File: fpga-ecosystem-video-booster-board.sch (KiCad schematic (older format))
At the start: 91 parts, among them J1 0473460001, J10 61300411121, J2 HDMI-PE10-19-LF, J3 HDMI-PE10-19-LF, J4 M20-9990246, J5 M20-9990246, J6 685119134923_, J7 M20-9990246, J8 M20-9990246, J9 685119134923_, Q1 BSS138-7-F, Q2 BSS138-7-F, U1 PTN3363, U2 EFM32HG309, U3 PTN3363, U4 LP2985-33DBVR

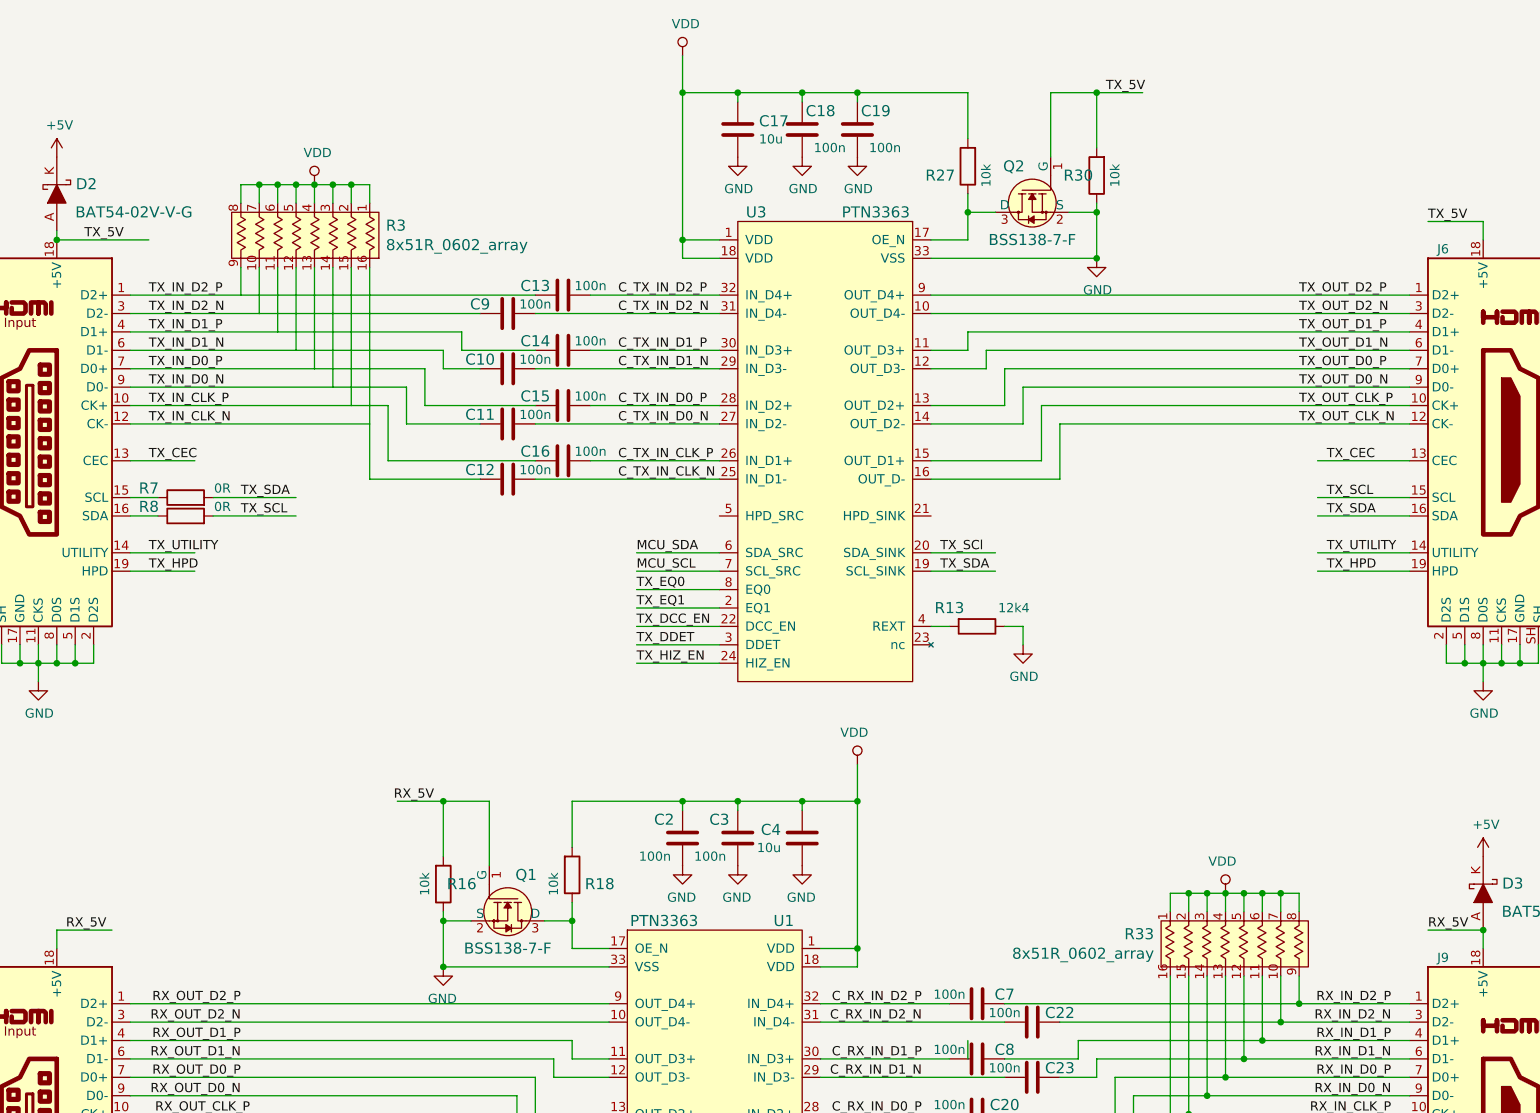
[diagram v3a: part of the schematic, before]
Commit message: Channels flipped for 1-side component placement
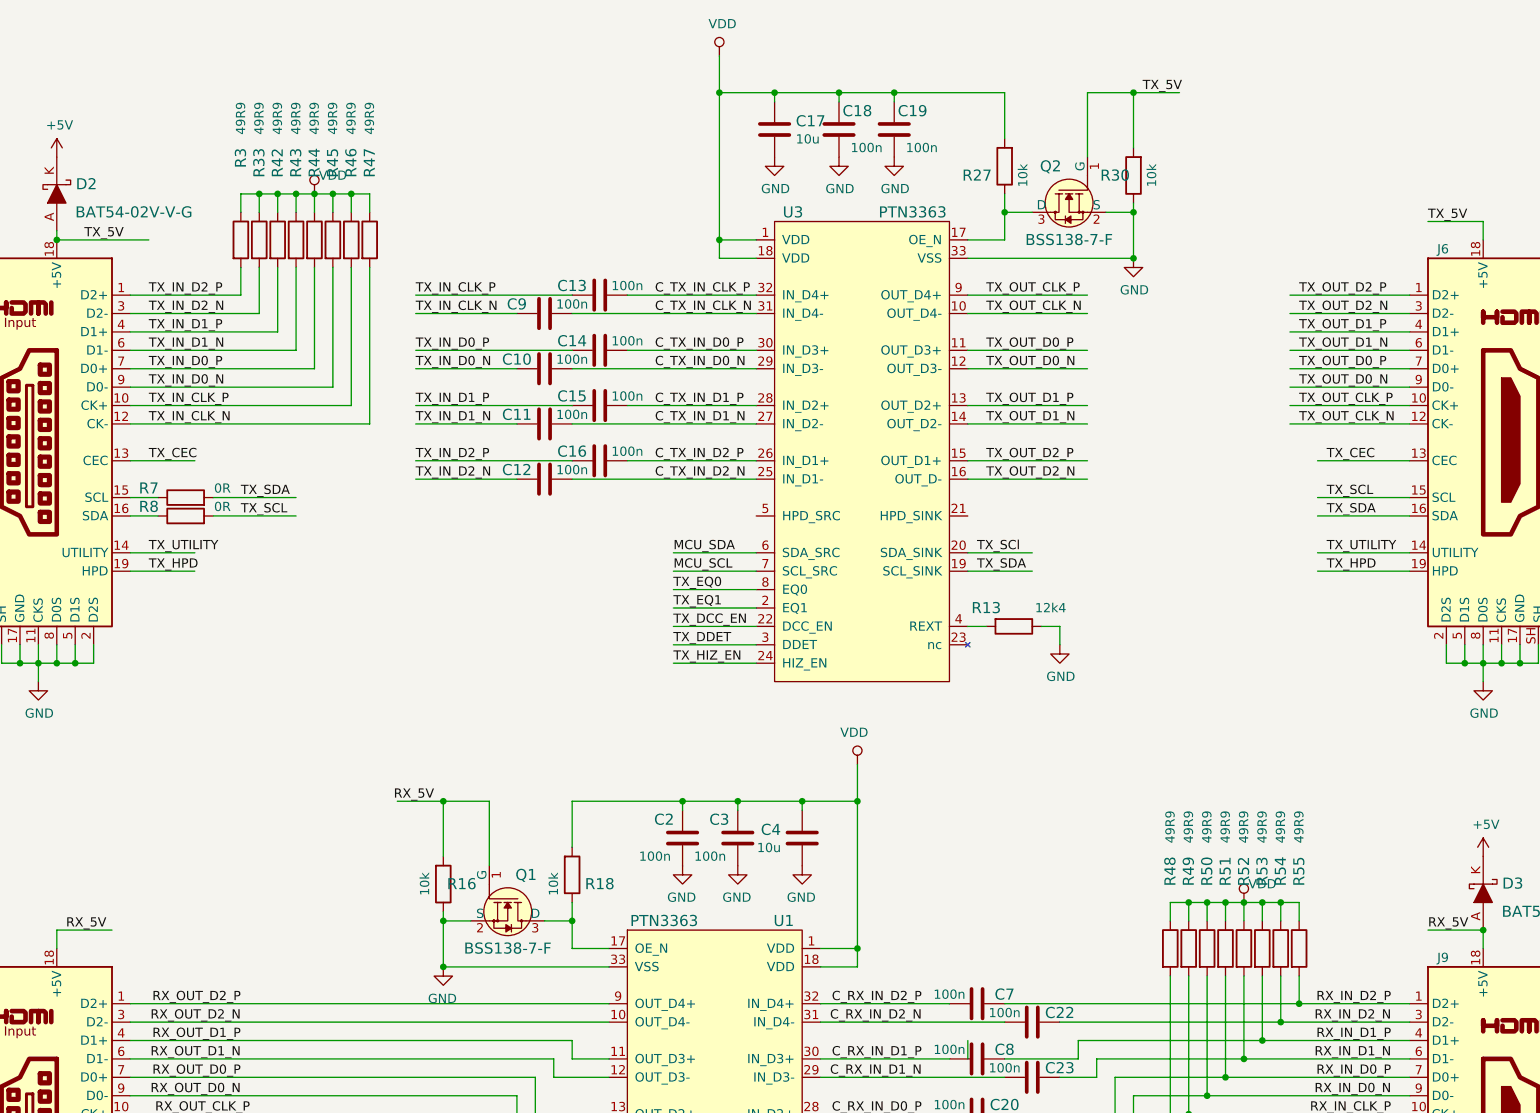
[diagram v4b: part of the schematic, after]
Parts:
- removed R3, R33: 8x51R_0602_array, antmicro-footprints:R_Array_Convex_8x0602, symbol antmicroResistorNetworksArrays:8x51R_0602_array
- added R3, R33, R42, R43, R44, R45, R46, R47, R48, R49, R50, R51, R52, R53, R54, R55: R_49R9_0402, antmicro-footprints:0402-res, symbol antmicroResistors0402:R_49R9_0402
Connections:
- wire segments 428 -> 414
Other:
- moved on the sheet: C10, C11, C12, C13, C14, C15, C16, C17, C18, C19, C9, Q2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

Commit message: Component layout for double, one sided dongle
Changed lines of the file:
@@
 	2100 3800 1950 3800
 Text Label 2550 7650 0    50   ~ 0
-TX_SCL
+RX_SCL
 Text Label 2550 7550 0    50   ~ 0
-TX_SDA
+RX_SDA
 $Comp
 L antmicroResistors0402:R_0R_0402 R11
